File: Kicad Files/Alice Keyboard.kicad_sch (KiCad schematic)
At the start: 153 parts, among them J1 0781710004, SW1 SW_Push, SW10 SW_Push, SW11 SW_Push, SW12 SW_Push, SW13 SW_Push, SW14 SW_Push, SW15 SW_Push, SW16 SW_Push, SW17 SW_Push, SW18 SW_Push, SW19 SW_Push, SW1L1 SW_SPST, SW2 SW_Push, SW20 SW_Push, SW21 SW_Push, SW22 SW_Push, SW23 SW_Push, SW24 SW_Push, SW25 SW_Push, SW26 SW_Push, SW27 SW_Push, SW28 SW_Push, SW29 SW_Push, SW2L1 SW_SPST, SW3 SW_Push, SW30 SW_Push, SW31 SW_Push, SW32 SW_Push, SW33 SW_Push, SW34 SW_Push, SW35 SW_Push, SW36 SW_Push, SW37 SW_Push, SW38 SW_Push, SW39 SW_Push, SW4 SW_Push, SW40 SW_Push, SW41 SW_Push, SW42 SW_Push, SW43 SW_Push, SW44 SW_Push, SW45 SW_Push, SW46 SW_Push, SW47 SW_Push, SW48 SW_Push, SW49 SW_Push, SW5 SW_Push, SW50 SW_Push, SW51 SW_Push, SW52 SW_Push, SW53 SW_Push, SW54 SW_Push, SW55 SW_Push, SW56 SW_Push, SW57 SW_Push, SW58 SW_Push, SW59 SW_Push, SW6 SW_Push, SW60 SW_Push, SW61 SW_Push, SW62 SW_Push, SW63 SW_Push, SW64 SW_Push, SW65 SW_Push, SW66 SW_Push, SW67 SW_Push, SW68 RotaryEncoder_Switch, SW7 SW_Push, SW8 SW_Push, SW9 SW_Push, U1 XC6206PxxxMR, U2 STM32F072CBTx

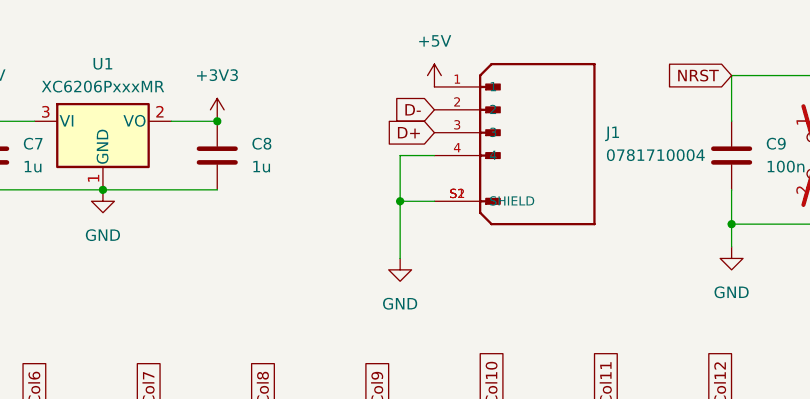
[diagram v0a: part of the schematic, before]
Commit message: Update kicad files
The old files had an issue with the D+ and D- lines being flipped the wrong way, this has rectified this.
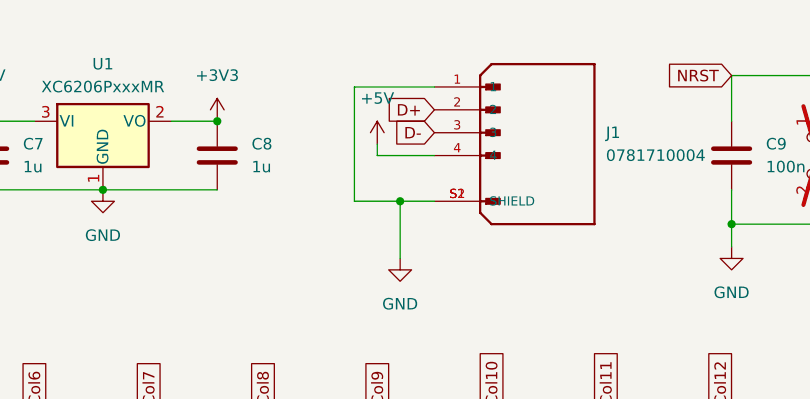
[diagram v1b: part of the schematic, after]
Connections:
- net +5V: now also J1.4; no longer J1.1
- net D+: now also J1.2; no longer J1.3
- net D-: now also J1.3; no longer J1.2
- net GND: now also J1.1; no longer J1.4
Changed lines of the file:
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@@
 	(wire
 		(pts
+			(xy 187.96 30.48) (xy 194.31 30.48)
+		)
+		(stroke
+			(width 0)
+			(type default)
+		)
+	)
+	(wire
+		(pts
 			(xy 187.96 87.63) (xy 187.96 106.68)
 		)
@@
 	(wire
 		(pts
+			(xy 185.42 22.86) (xy 194.31 22.86)
+		)
+		(stroke
+			(width 0)
+			(type default)
+		)
+	)
+	(wire
+		(pts
 			(xy 190.5 132.08) (xy 203.2 132.08)
 		)
@@
 	(wire
 		(pts
-			(xy 190.5 30.48) (xy 194.31 30.48)
-		)
-		(stroke
-			(width 0)
-			(type default)
-		)
-	)
-	(wire
-		(pts
 			(xy 109.22 25.4) (xy 118.11 25.4)
 		)
@@
 	(wire
 		(pts
-			(xy 190.5 35.56) (xy 190.5 30.48)
-		)
-		(stroke
-			(width 0)
-			(type default)
-		)
-	)
-	(wire
-		(pts
 			(xy 266.7 148.59) (xy 273.05 148.59)
 		)
@@
 	(wire
 		(pts
+			(xy 185.42 22.86) (xy 185.42 35.56)
+		)
+		(stroke
+			(width 0)
+			(type default)
+		)
+	)
+	(wire
+		(pts
 			(xy 165.1 77.47) (xy 177.8 77.47)
 		)
@@
 	(wire
 		(pts
+			(xy 185.42 35.56) (xy 190.5 35.56)
+		)
+		(stroke
+			(width 0)
+			(type default)
+		)
+	)
+	(wire
+		(pts
 			(xy 190.5 41.91) (xy 190.5 35.56)
 		)
@@
 	(wire
 		(pts
+			(xy 187.96 29.21) (xy 187.96 30.48)
+		)
+		(stroke
+			(width 0)
+			(type default)
+		)
+	)
+	(wire
+		(pts
 			(xy 44.45 107.95) (xy 46.99 107.95)
 		)
@@
 	(global_label "D-"
 		(shape input)
-		(at 194.31 25.4 180)
+		(at 194.31 27.94 180)
 		(fields_autoplaced yes)
 		(effects
@@
 		)
 		(property "Intersheetrefs" "${INTERSHEET_REFS}"
-			(at 188.4824 25.4 0)
+			(at 188.4824 27.94 0)
 			(effects
 				(font
@@
 	(global_label "D+"
 		(shape input)
-		(at 194.31 27.94 180)
+		(at 194.31 25.4 180)
 		(fields_autoplaced yes)
 		(effects
@@
 		)
 		(property "Intersheetrefs" "${INTERSHEET_REFS}"
-			(at 188.4824 27.94 0)
+			(at 188.4824 25.4 0)
 			(effects
 				(font
@@
 	(symbol
 		(lib_id "power:+5V")
-		(at 194.31 22.86 0)
+		(at 187.96 29.21 0)
 		(unit 1)
 		(exclude_from_sim no)
@@
 		(fields_autoplaced yes)
 		(property "Reference" "#PWR02"
-			(at 194.31 26.67 0)
+			(at 187.96 33.02 0)
 			(effects
 				(font
@@
 		)
 		(property "Value" "+5V"
-			(at 194.31 17.78 0)
+			(at 187.96 24.13 0)
 			(effects
 				(font
@@
 		)
 		(property "Footprint" ""
-			(at 194.31 22.86 0)
+			(at 187.96 29.21 0)
 			(effects
 				(font
@@
 		)
 		(property "Datasheet" ""
-			(at 194.31 22.86 0)
+			(at 187.96 29.21 0)
 			(effects
 				(font
@@
 		)
 		(property "Description" ""
-			(at 194.31 22.86 0)
+			(at 187.96 29.21 0)
 			(effects
 				(font
